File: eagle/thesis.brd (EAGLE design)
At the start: 100 x 62.1 mm, 14 parts, among them J1 RJ11-6PTH, U1 ITG-3200, U2 ADXL362

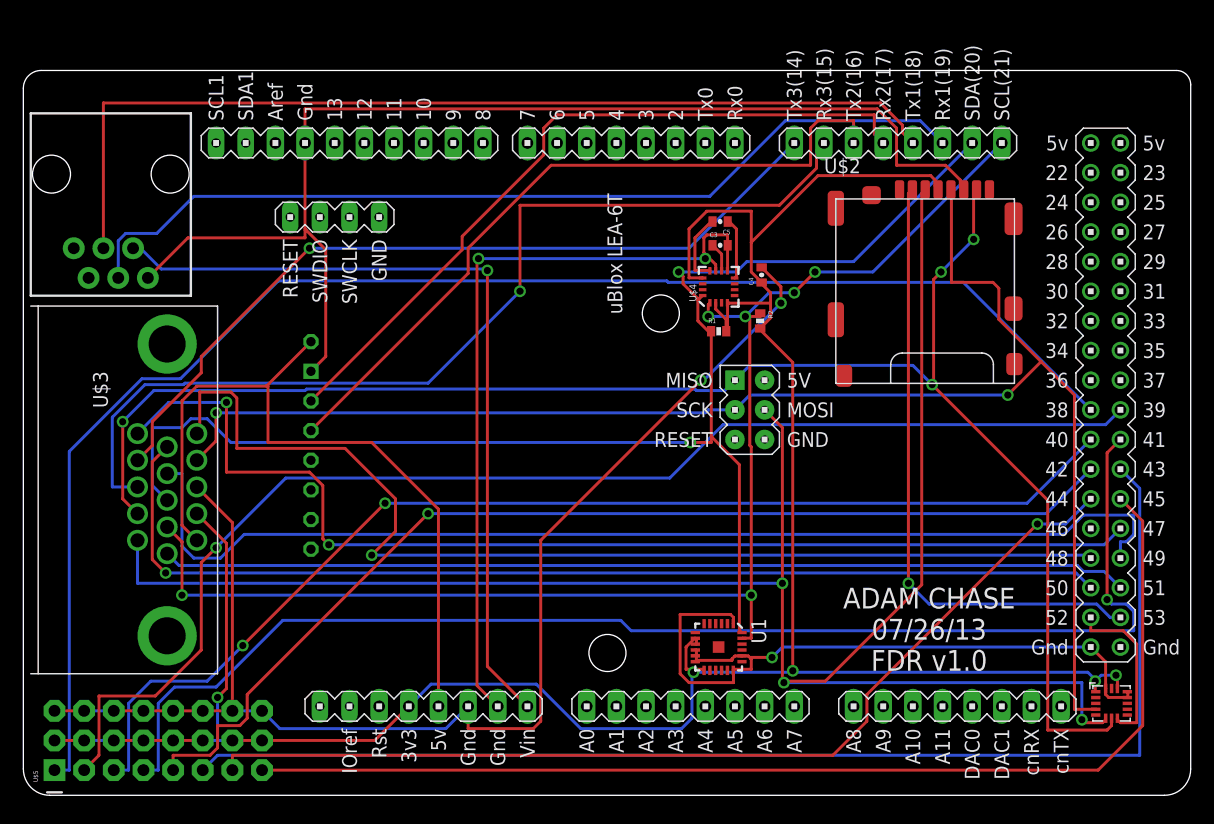
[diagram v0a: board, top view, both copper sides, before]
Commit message: eagle file changes that were submitted for a quote
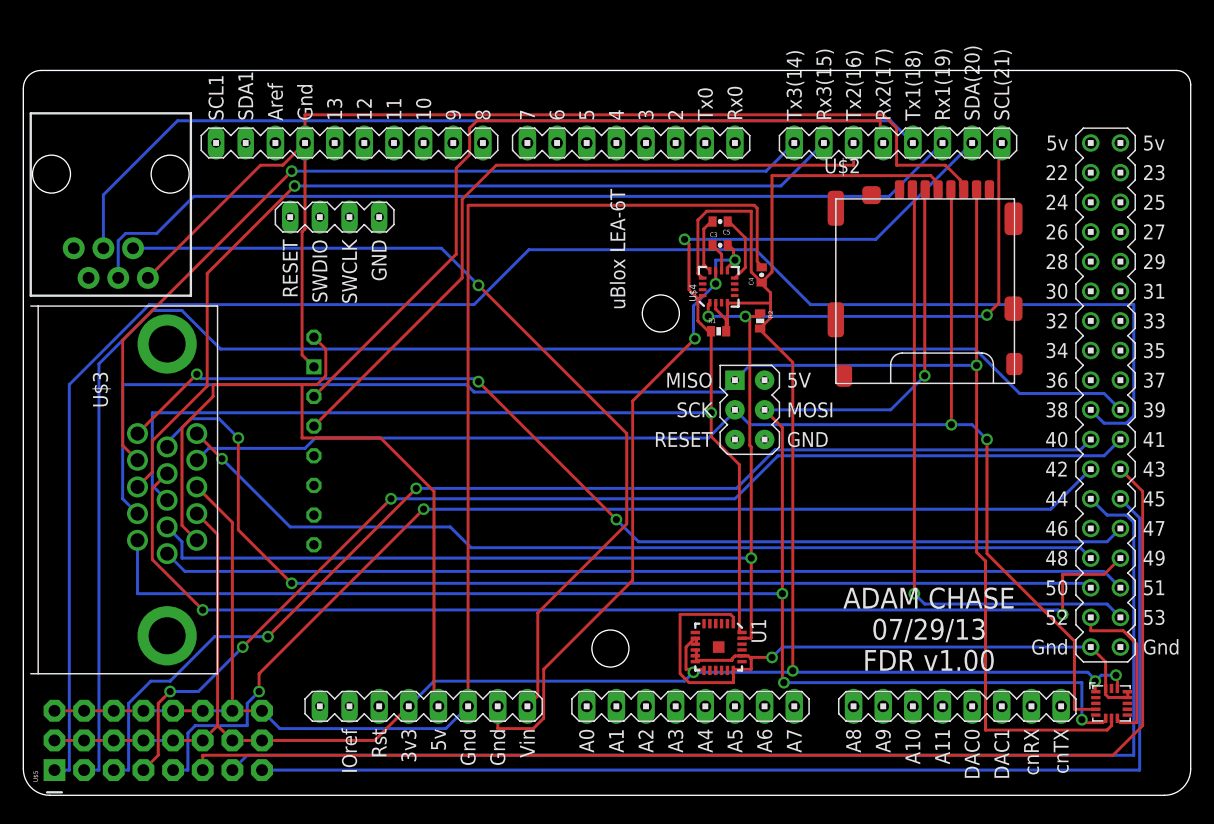
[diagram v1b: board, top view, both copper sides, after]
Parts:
- moved U$6 0.46 mm to (22.4, 53.2)
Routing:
- net N$2: track 108.9 -> 129.0 mm, vias 1 -> 0
- net N$1: track 126.7 -> 146.2 mm
- net MOSI: track 163.5 -> 146.0 mm, vias 3 -> 4
- net N$9: track 85.2 -> 102.2 mm, vias 1 -> 0
- net GND1: track 113.9 -> 130.3 mm, vias 2 -> 0
- net N$4: track 112.4 -> 98.0 mm, vias 1 -> 3
- net D48: track 94.1 -> 81.0 mm
- net SCLK: track 130.0 -> 118.8 mm
- net GND2: track 67.3 -> 57.4 mm, vias 2 -> 3
- net TX1: track 83.6 -> 77.3 mm
- net VIN: track 69.9 -> 75.8 mm
- net TX3: track 69.5 -> 75.3 mm
- net RX3: track 84.0 -> 78.2 mm
- net MISO: track 138.9 -> 144.1 mm, vias 4 -> 1
- net SCL: track 117.6 -> 122.3 mm, vias 6 -> 4
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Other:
- board text added: "ADAM CHASE 07/29/13 FDR v1.00"
- board text removed: "ADAM CHASE 07/26/13 FDR v1.0"

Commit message: made board revision to v2.0 and ready to order, pending BOM
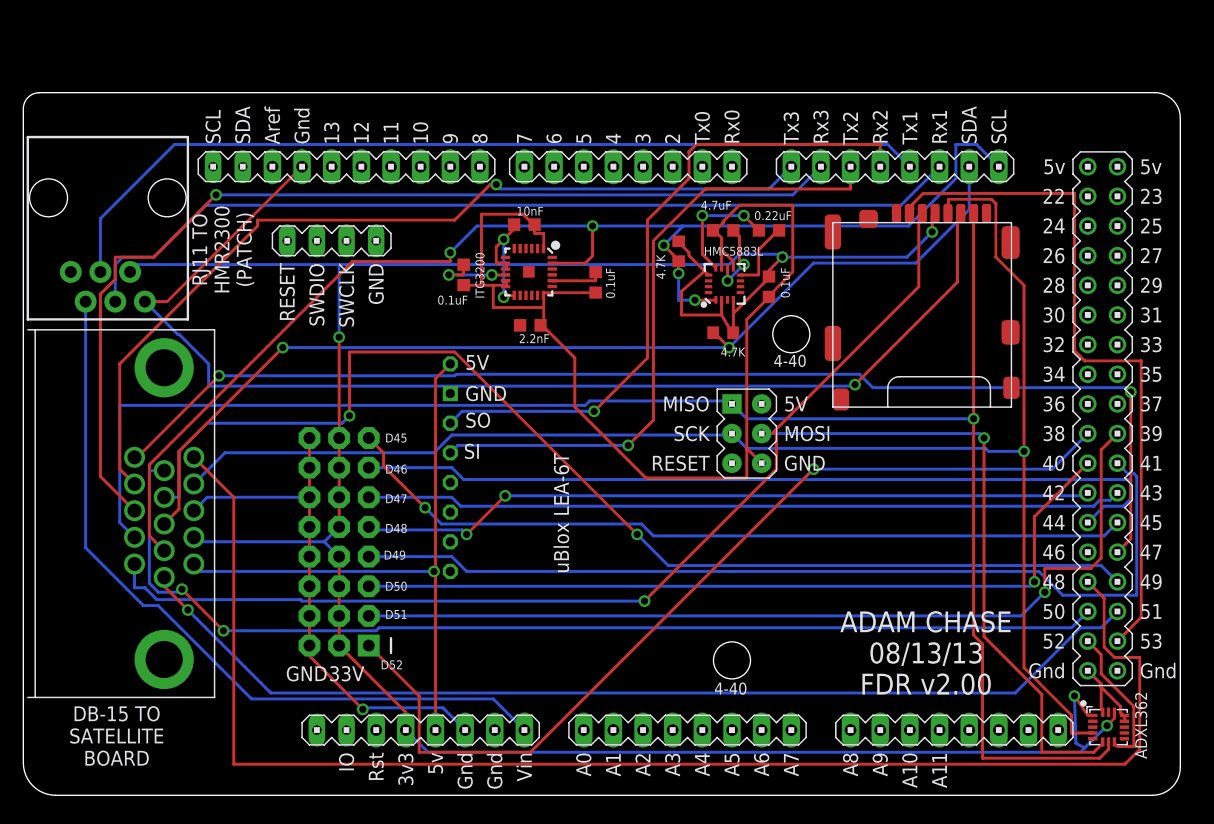
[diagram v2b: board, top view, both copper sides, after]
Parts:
- added C1, C6: 0.1uF, rcl:C0603K
- added C2: 2.2nF, rcl:C0603K
- added C7: 10nF, rcl:C0603K
- C3, C4, C5: device HMC5883L_Breakout-v11:SPARKFUN_0402-CAP -> rcl:C0603K
- R1, R2: device HMC5883L_Breakout-v11:SPARKFUN_0402-RES -> rcl:R0603
- moved U1 36.0 mm to (43.3, 44.8)
- moved U$5 24.8 mm to (28.3, 21.7), turned to 180 degrees
- moved U$6 11.9 mm to (34.0, 50.9)
- moved R2 9.19 mm to (56.1, 46.6), turned to 90 degrees
- moved C5 4.26 mm to (63.9, 48.4)
- moved U$2 2.05 mm to (76.8, 41.7)
- moved J1 2.05 mm to (12.3, 51.2)
- moved U$1 2.05 mm to (72.1, 23.4)
- moved U2 2.05 mm to (93.0, 5.84)
- moved U$3 2.05 mm to (0.38, 24.1)
- moved C3 1.30 mm to (59.9, 48.4), turned to 180 degrees
- moved C4 1.20 mm to (63.9, 43.6), turned to 270 degrees
- moved U$4 0.57 mm to (60.1, 43.8)
- moved R1 0.40 mm to (59.9, 39.6)
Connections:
- net N$1 renamed D38
- net N$10 renamed D45
- net N$2 renamed D39
- net N$3 renamed D40
- net N$4 renamed D41
- net N$6 renamed D42
- net N$8 renamed D43
- net N$9 renamed D44
- new net CPOUT: C2.2, U1.20
- new net GNDHEAD: C1.1, C2.1, C3.2, C4.2, C6.1, C7.1, U$1.5V_ICSP, U$4.11, U$4.9, U1.1, U1.11, U1.12, U1.18
- new net N$14: C1.2, U1.10
- net 33V: now also C7.2, J1.2
- net GND1: no longer C4.2
- net GND2: no longer C3.2, U$4.11, U$4.9
- net GNDA: no longer U1.1, U1.10, U1.11, U1.12, U1.18, U1.20
- net VIN: now also J1.5; no longer J1.2
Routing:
- net GNDHEAD: track 0.00 -> 97.5 mm
- net GND1: track 130.3 -> 45.1 mm, vias 0 -> 1
- net D38: track 146.2 -> 79.5 mm, vias 0 -> 1
- net GND2: track 57.4 -> 0.00 mm, vias 3 -> 0
- net GNDA: track 61.8 -> 7.91 mm, vias 1 -> 0
- net D39: track 129.0 -> 77.2 mm, vias 0 -> 1
- net D48: track 81.0 -> 123.3 mm, vias 1 -> 0
- net D43: track 105.6 -> 64.9 mm
- net SDA: track 120.4 -> 88.6 mm
- net D45: track 99.1 -> 68.7 mm, vias 0 -> 1
- net D44: track 102.2 -> 71.9 mm
- net D42: track 93.2 -> 63.3 mm
- net D40: track 98.8 -> 69.2 mm, vias 2 -> 1
- net 33V: track 206.9 -> 233.2 mm, vias 4 -> 7
- net D41: track 98.0 -> 79.4 mm, vias 3 -> 0
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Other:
- board size 100 x 62.1 mm -> 99.1 x 60.2 mm
- board text added: "0.1uF"
- board text added: "0.22uF"
- board text added: "10nF"
- board text added: "2.2nF"
- board text added: "33V"
- board text added: "4-40"
- board text added: "4.7K"
- board text added: "4.7uF"
- board text added: "5V"
- board text added: "ADAM CHASE 08/13/13 FDR v2.00"
- board text added: "ADXL362"
- board text added: "CAL POLY FLIGHT LAB"
- board text added: "D45"
- board text added: "D46"
- board text added: "D47"
- board text added: "D48"
- board text added: "D49"
- board text added: "D50"
- board text added: "D51"
- board text added: "D52"
- board text added: "DB-15 TO SATELLITE BOARD"
- board text added: "GND"
- board text added: "HMC5883L"
- board text added: "ITG3200"
- board text added: "RJ11 TO HMR2300 (PATCH)"
- board text added: "SI"
- board text added: "SO"
- board text removed: "ADAM CHASE 07/29/13 FDR v1.00"
